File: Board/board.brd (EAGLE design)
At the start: 129 x 93.4 mm, 51 parts, among them IC1 L297, IC2 MEGA32-P, IC3 L298, J1 +12V, Q1 BC639, Q3 BC639, U2 DS1621+, X1 WATER_PUMP, X2 FAN, X5 SM_CD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

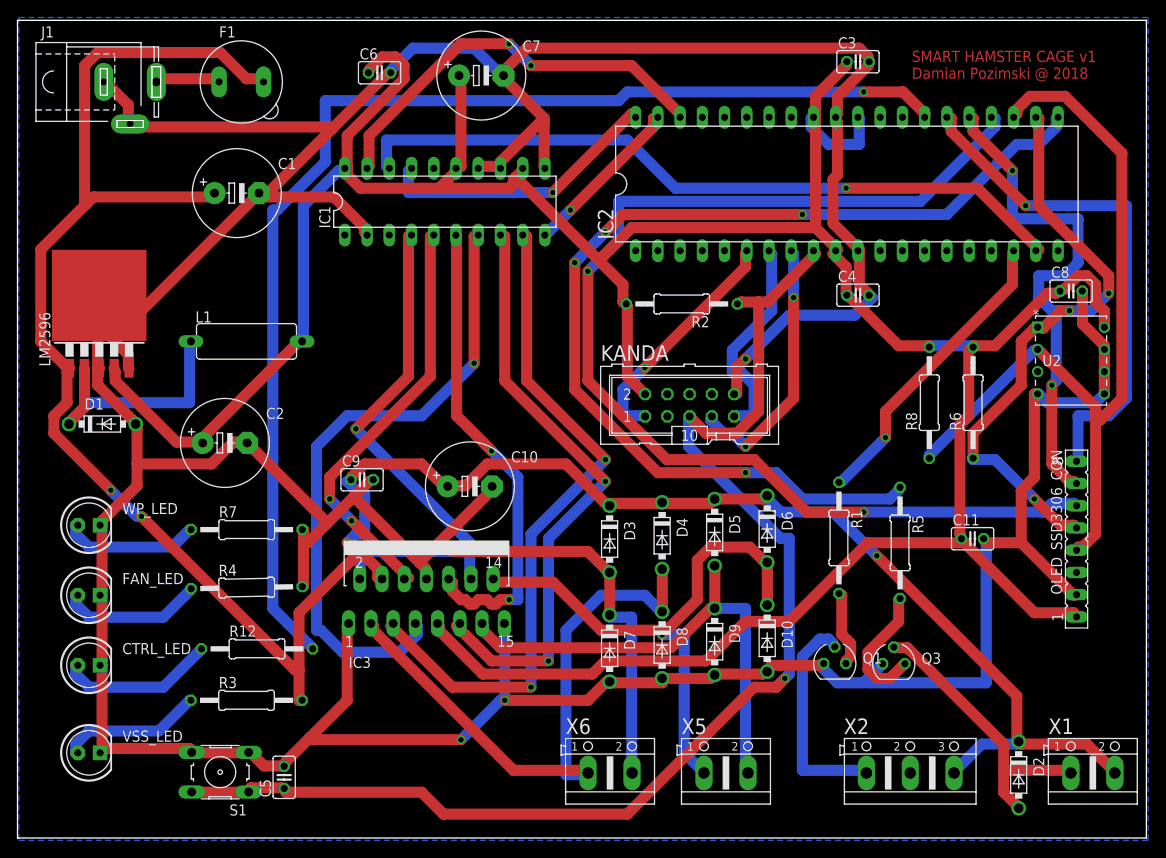
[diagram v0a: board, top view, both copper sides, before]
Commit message: SCL/SDA thermometer
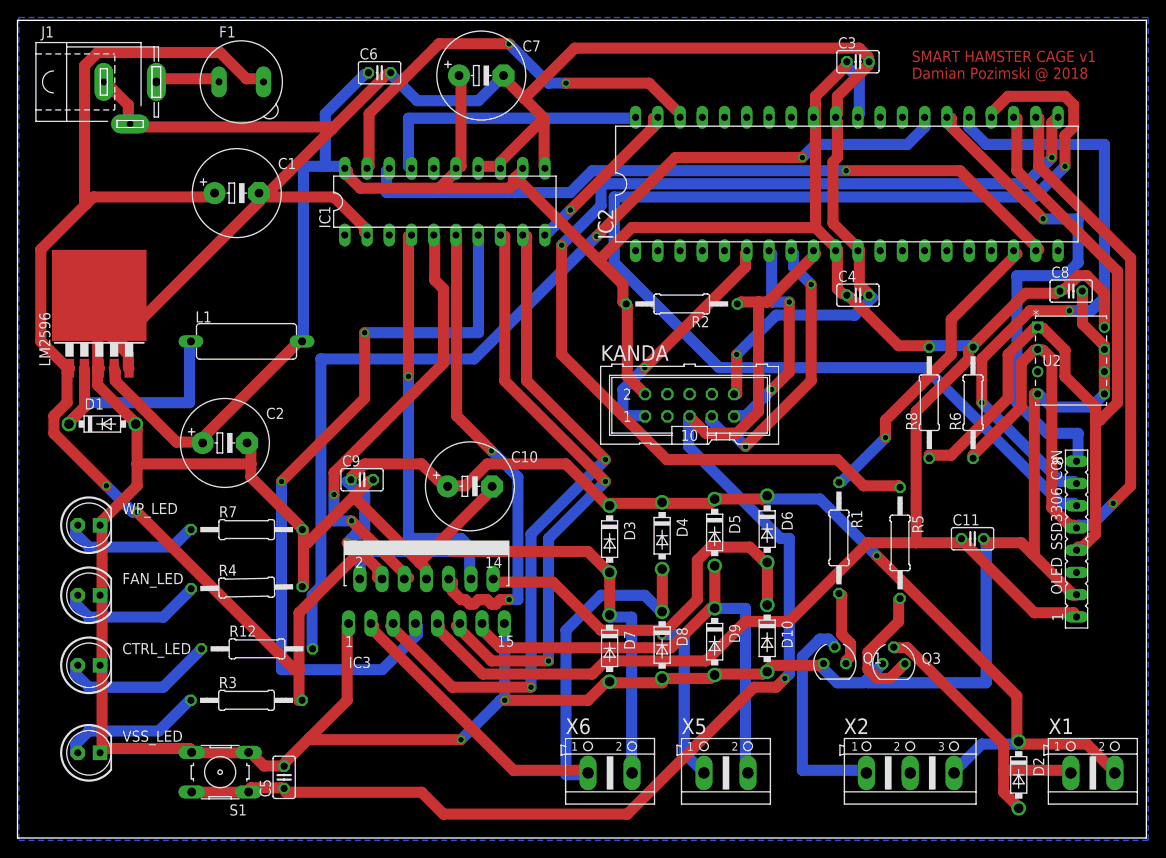
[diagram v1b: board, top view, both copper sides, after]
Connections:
- net N$35: now also U2.1; no longer U2.2
- net N$36: now also U2.2; no longer U2.1
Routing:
- net N$36: track 66.8 -> 93.4 mm, vias 3 -> 1
- net N$11: track 137.6 -> 114.6 mm, vias 1 -> 2
- net N$38: track 57.7 -> 71.5 mm
- net N$56: track 72.6 -> 85.1 mm, vias 1 -> 2
- net N$37: track 132.4 -> 143.3 mm, vias 2 -> 1
- net VCC: track 357.2 -> 351.8 mm
- net GND: track 569.8 -> 564.8 mm
- net N$12: track 120.1 -> 124.0 mm, vias 4 -> 2
- net N$4: track 30.4 -> 32.1 mm
- net N$15: track 48.4 -> 50.0 mm
- net N$20: track 47.4 -> 48.9 mm
- net N$16: track 47.4 -> 46.0 mm
- net N$17: track 32.8 -> 31.9 mm, vias 1 -> 0
- net N$18: track 83.4 -> 82.5 mm
- net N$35: track 93.0 -> 92.3 mm
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
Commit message: Rename 1N5824 - 1N5822
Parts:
- D2: value 1N5824 -> 1N5822
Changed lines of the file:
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@@
 <attribute name="SPICEPREFIX" value="R" x="16.02" y="-93.13" size="1.778" layer="27" rot="R1.1" display="off"/>
 </element>
-<element name="D2" library="diode" package="DO41-7.6" value="1N5824" x="104.21" y="-114.52" rot="R270"/>
+<element name="D2" library="diode" package="DO41-7.6" value="1N5822" x="104.21" y="-114.52" rot="R270"/>
 <element name="R5" library="rcl" package="0207/12" value="240R" x="90.66" y="-88.02" rot="R270">
 <attribute name="SPICEPREFIX" value="R" x="107.17" y="-88.02" size="1.778" layer="27" rot="R270" display="off"/>

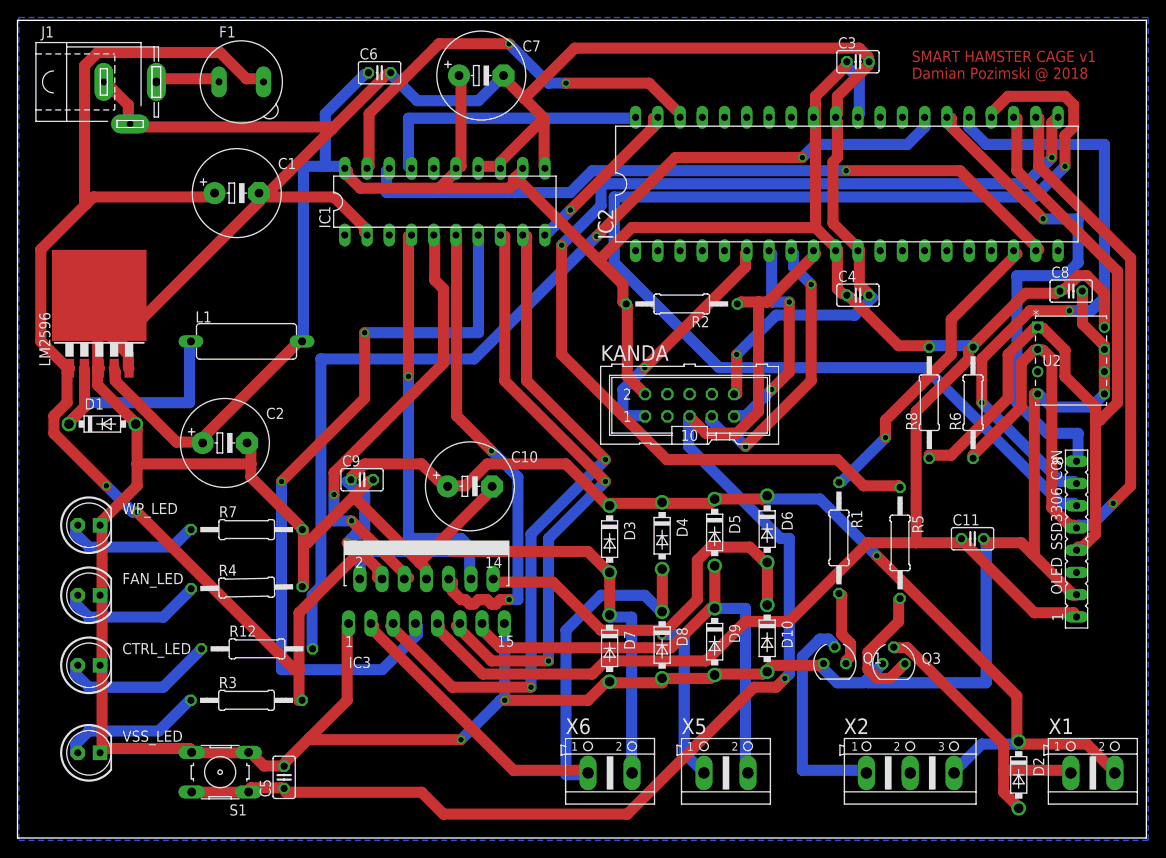
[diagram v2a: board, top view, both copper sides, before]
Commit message: AREF cannot be connected to VCC
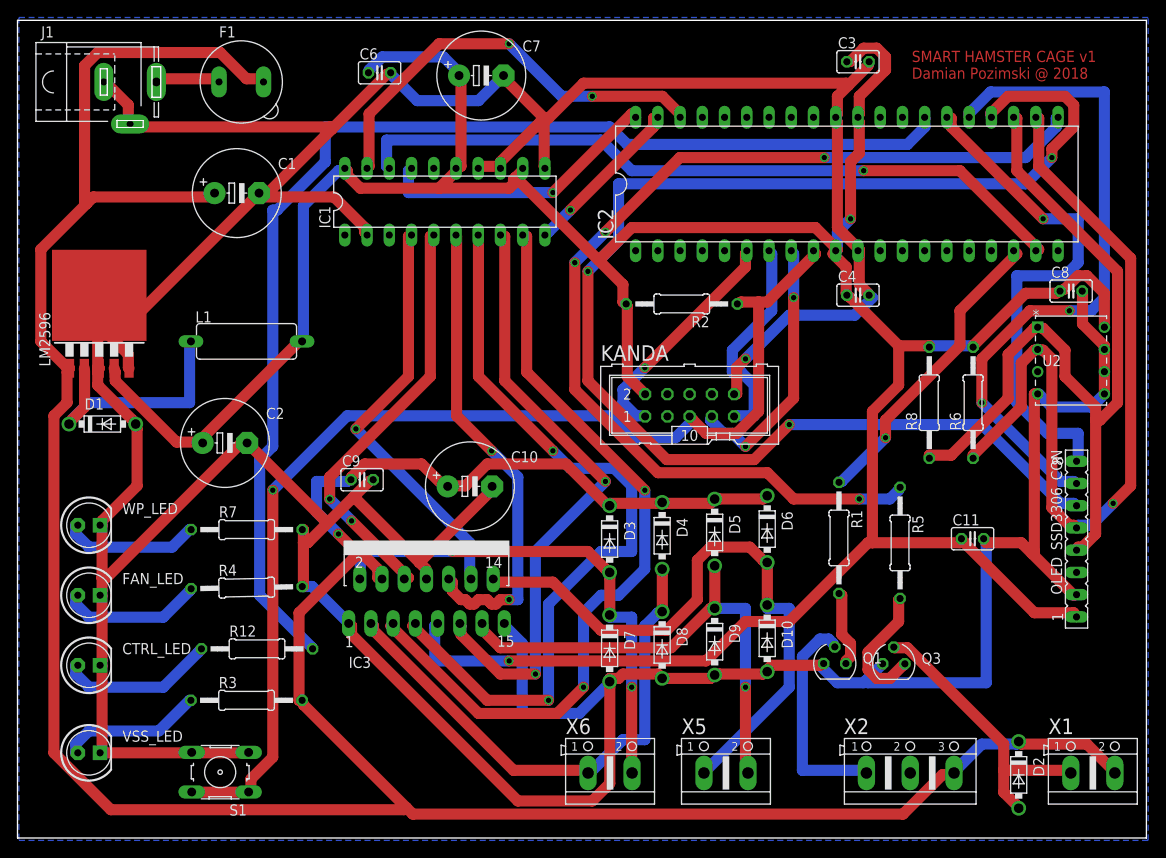
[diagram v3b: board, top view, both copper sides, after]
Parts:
- removed C5: 100nF, rcl:C025-025X050
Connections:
- new net AREF: IC2.32
- net GND: no longer C5.2
- net N$10: no longer C5.1
- net VCC: no longer IC2.32
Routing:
- net VSS: track 276.9 -> 358.5 mm, vias 4 -> 1
- net N$11: track 114.6 -> 136.8 mm, vias 2 -> 0
- net GND: track 564.8 -> 583.3 mm, vias 3 -> 1
- net N$10: track 145.2 -> 130.0 mm
- net N$37: track 143.3 -> 157.9 mm, vias 1 -> 3
- net N$13: track 78.5 -> 89.4 mm
- net N$26: track 69.8 -> 60.8 mm
- net N$24: track 65.6 -> 71.6 mm, vias 1 -> 0
- net N$38: track 71.5 -> 77.0 mm
- net N$12: track 124.0 -> 120.1 mm, vias 2 -> 4
- net N$56: track 85.1 -> 88.7 mm
- net N$4: track 32.1 -> 30.4 mm
- net N$15: track 50.0 -> 48.4 mm
- net N$16: track 46.0 -> 47.4 mm
- net N$21: track 69.1 -> 70.3 mm
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
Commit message: 10mil for corners
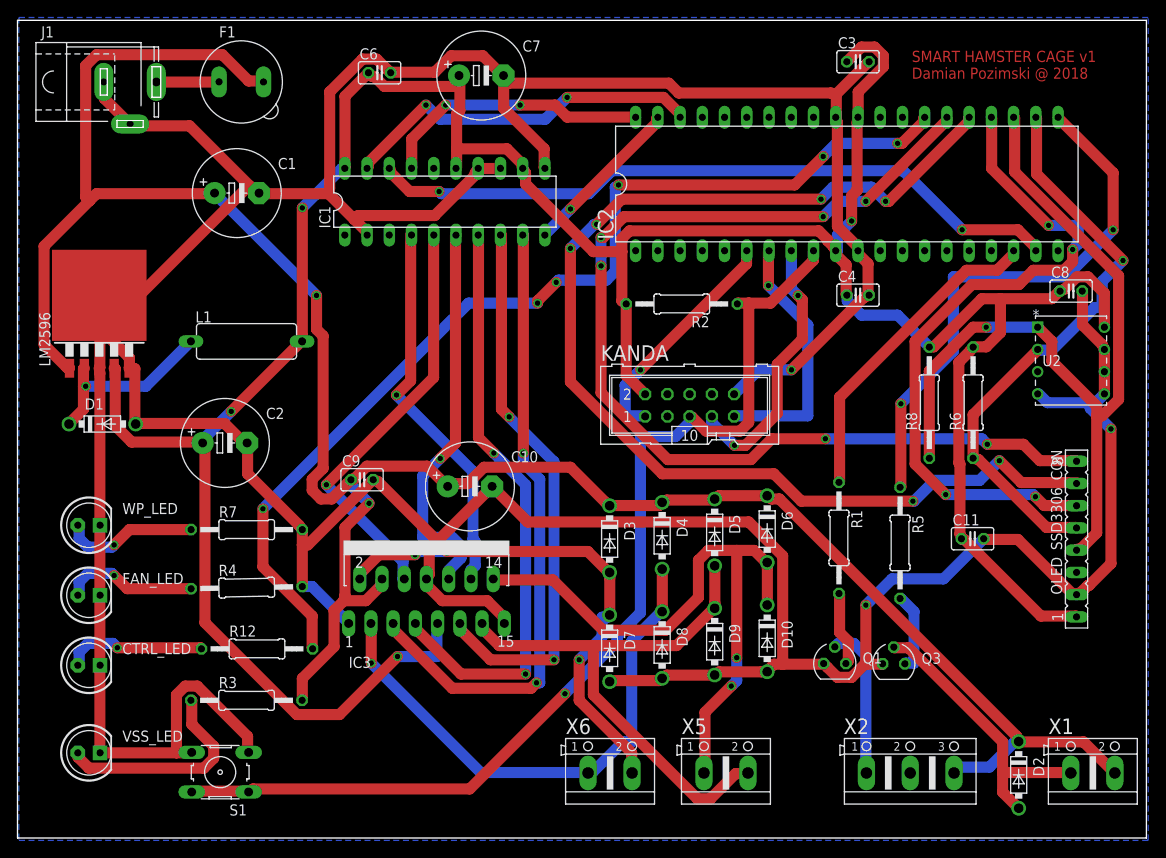
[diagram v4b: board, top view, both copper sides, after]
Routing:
- net VSS: track 358.5 -> 269.4 mm, vias 1 -> 2
- net N$37: track 157.9 -> 79.0 mm, vias 3 -> 4
- net N$39: track 59.2 -> 122.7 mm, vias 1 -> 6
- net N$38: track 77.0 -> 135.1 mm, vias 2 -> 6
- net N$12: track 120.1 -> 62.5 mm, vias 4 -> 2
- net N$36: track 93.4 -> 66.8 mm
- net N$56: track 88.7 -> 67.7 mm
- net N$11: track 136.8 -> 118.5 mm, vias 0 -> 6
- net N$13: track 89.4 -> 72.4 mm
- net GND: track 583.3 -> 571.0 mm, vias 1 -> 3
- net VCC: track 351.0 -> 340.9 mm, vias 2 -> 4
- net N$58: track 54.8 -> 45.3 mm, vias 2 -> 1
- net N$10: track 130.0 -> 120.7 mm
- net N$7: track 16.5 -> 24.8 mm
- net N$9: track 25.4 -> 17.7 mm
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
